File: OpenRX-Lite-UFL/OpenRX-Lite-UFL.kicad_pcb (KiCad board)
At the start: 6 copper layers, 10 x 11.5 mm, 47 parts, among them J1 Conn_Coaxial, U1 ESP32-C3, U2 TLV75533PDQNR, U3 SX1281IMLTRT, X1 CJ17-400001010B20

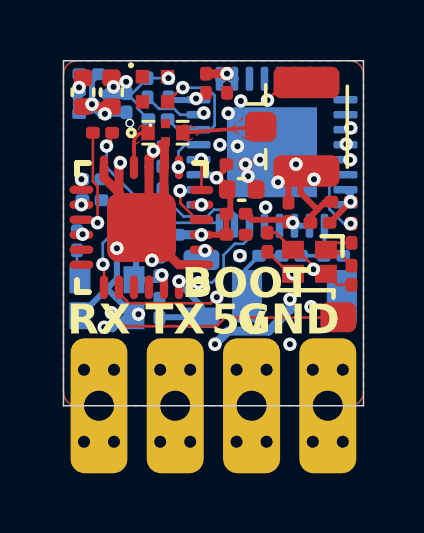
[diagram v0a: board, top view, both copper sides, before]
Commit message: Rev 2 board work: routing optimisations, logo placement, 3D model fixes
Routing reworked on Lite (segments 313 to 256, vias 60 to 89), Lite-UFL
(317 to 269, 61 to 85) and Gemini (682 to 688, 196 to 243). ExpressLRS logo
placed on Mono.

3D model fixes on Gemini and Mono:

- RFX2401C (U4, U7) pointed at QFN-16_L3.0-W3.0-H0.9-P0.50.wrl with an offset
  of (-951.61, 821.31, 0), so the body rendered about a metre off the board and
  the land looked bare in the viewer. Repointed at the RFX2401C model that
  OpenRX-Shared.pretty/QFN-16_L3.0-W3.0-P0.50-BL-EP1.7.kicad_mod specifies,
  offset zeroed, 270 degree rotation kept.
- SKY13373 (U5, U8) carried no model reference at all. Added, matching the
  library footprint.

The boards now agree with the shared library on both, so Update Footprints from
Library preserves this rather than reverting it.

DRC reviewed: zero unconnected items on all four boards. The remaining items
are pre-existing and understood. The shorting_items reports on Lite and
Lite-UFL are all netted-copper against unnetted copper inside the multi-hole
TP footprints, never signal to signal, and are present at the previous commit
too. The copper_edge_clearance reports are the TP1-TP4 castellated pads sitting
on the board edge by design.

Co-Authored-By: Claude Opus 5 (1M context) <noreply@anthropic.com>
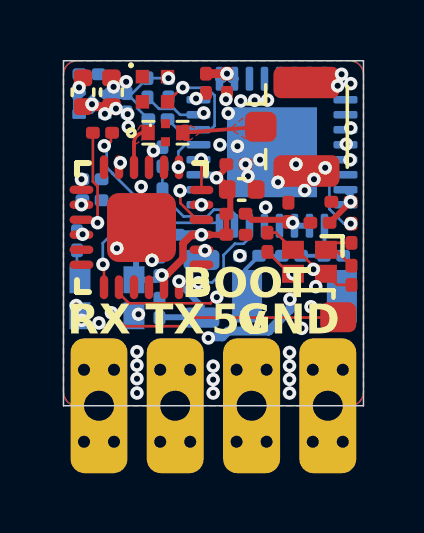
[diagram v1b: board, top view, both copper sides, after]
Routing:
- net GND: track 32.1 -> 5.33 mm, vias 25 -> 49
- net +3V3: track 22.3 -> 24.7 mm
